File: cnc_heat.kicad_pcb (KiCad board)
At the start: 2 copper layers, 56.4 x 80 mm, 55 parts, among them J1 Raspberry_Pi_2_3, J2 DB25_Receptacle_MountingHoles, U1 74LVC1T45, U10 74LVC1T45, U11 74LVC1T45, U12 74LVC1T45, U13 74LVC1T45, U14 74LVC1T45, U15 74LVC1T45, U16 74LVC1T45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

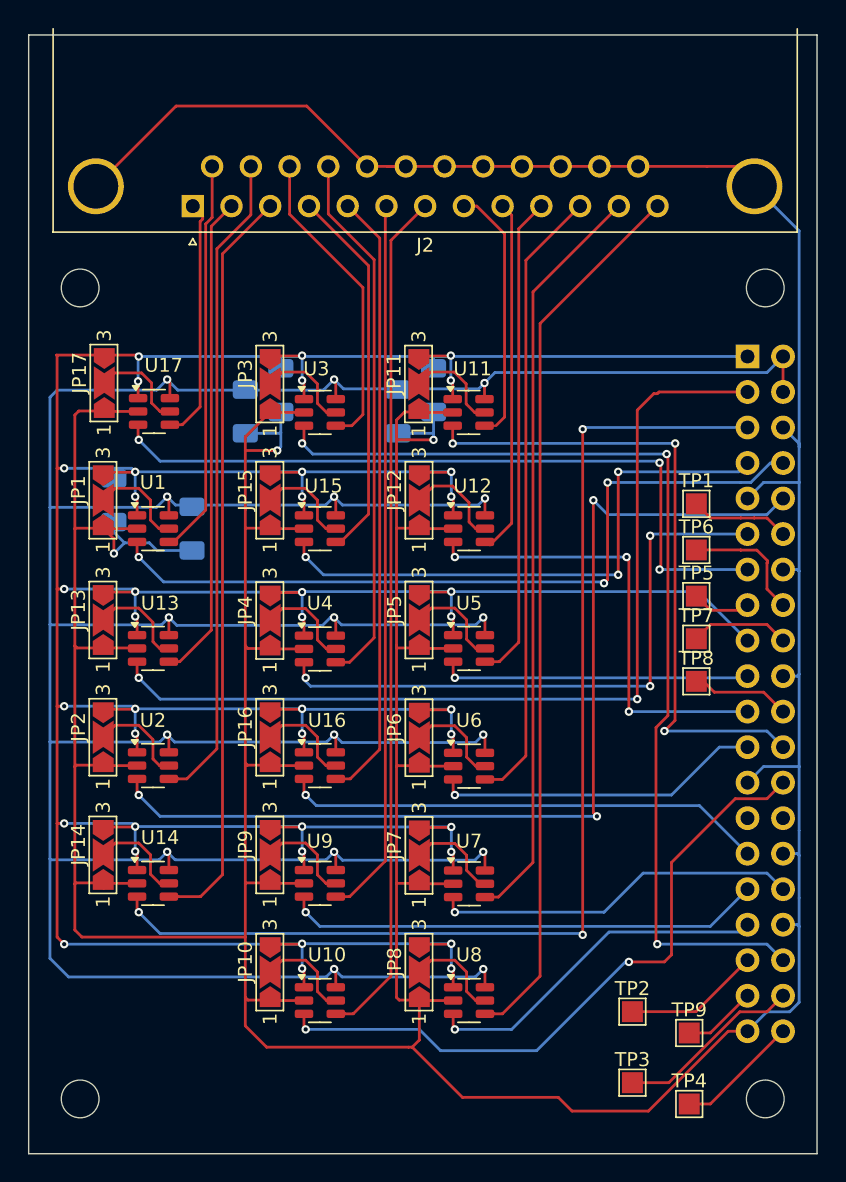
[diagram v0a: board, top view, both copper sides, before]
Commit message: routing cleanup
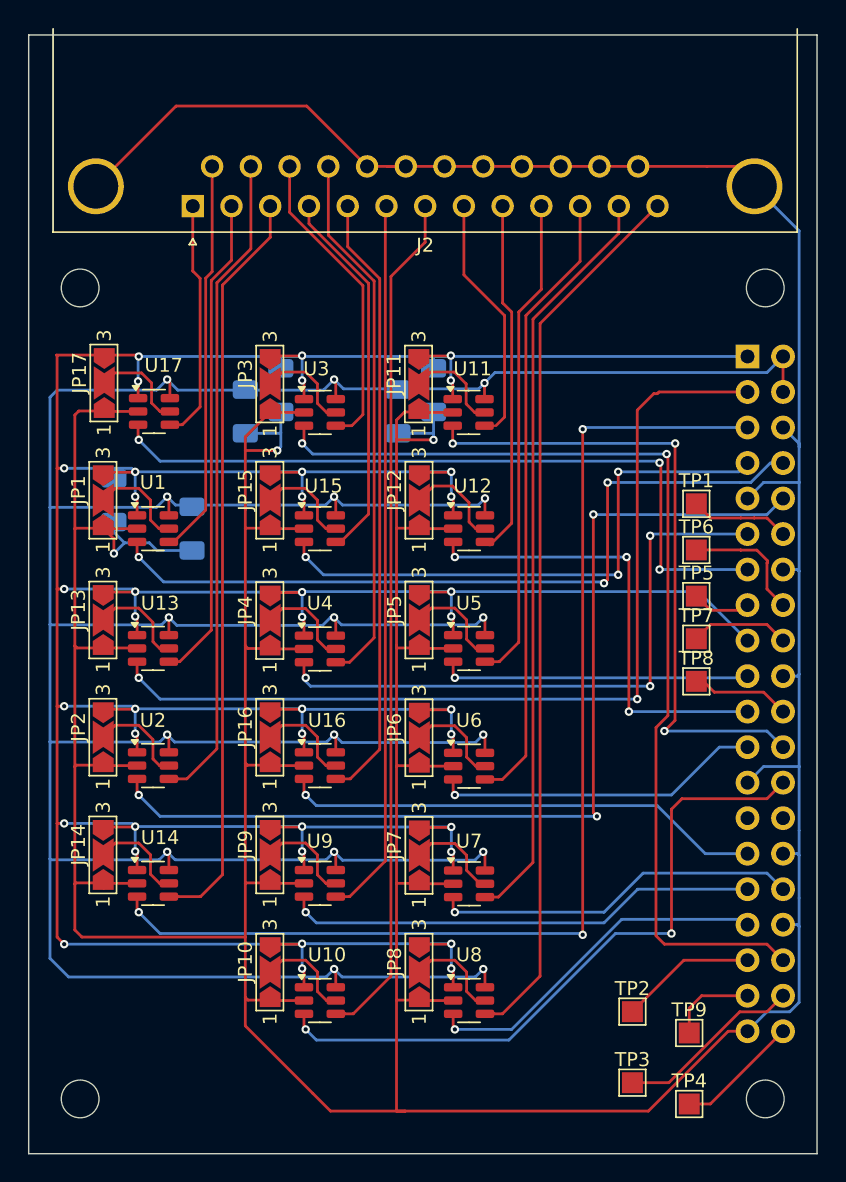
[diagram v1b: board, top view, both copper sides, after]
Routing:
- net GND: track 408.9 -> 414.0 mm
- net 15A: track 71.8 -> 70.3 mm
- net Net-(J1-GPIO26): track 5.27 -> 6.31 mm
- net 7A: track 47.7 -> 48.5 mm
- net 8B: track 18.4 -> 17.8 mm
- net 16A: track 72.7 -> 72.4 mm, vias 3 -> 2

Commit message: ocd routing
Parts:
- moved C6 43.1 mm to (77.5, 98.0)
- moved C5 37.5 mm to (77.5, 89.7)
- moved C4 24.4 mm to (77.5, 81.3)
- moved C3 18.1 mm to (77.5, 72.9)
- moved C1 10.6 mm to (77.5, 55.9)
- moved TP2 5.79 mm to (111.5, 96.3)
- moved TP3 5.11 mm to (111.5, 102.6)
- moved C2 2.27 mm to (77.5, 64.3)
- moved TP9 2.09 mm to (111.5, 99.3)
- moved TP4 0.92 mm to (111.5, 105.7)
- renumbered C5 to C1, C1 to C2, C6 to C3, C2 to C4, C7 to C5, C3 to C6
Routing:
- net GND: track 414.0 -> 405.3 mm, vias 3 -> 6
- net +5V: track 281.7 -> 288.1 mm
- net Net-(J1-GPIO19/MISO1): track 9.76 -> 3.71 mm
- net Net-(J1-GPIO20/MOSI1): track 13.3 -> 7.83 mm
- net 13B: track 64.3 -> 66.9 mm
- net Net-(J1-GPIO26): track 6.31 -> 3.92 mm
- net +3V3: track 348.8 -> 347.2 mm
- net 12B: track 53.9 -> 55.3 mm
- net 16A: track 72.4 -> 71.1 mm
- net 9B: track 25.5 -> 26.7 mm
- net 8A: track 47.0 -> 45.8 mm
- net 7B: track 61.8 -> 62.8 mm
- net 6B: track 51.5 -> 52.5 mm
- net Net-(JP2-C): track 7.06 -> 8.04 mm
- net Net-(JP14-C): track 7.06 -> 7.90 mm
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
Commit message: ocd routing
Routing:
- net 1A: track 53.7 -> 52.9 mm
- net 14A: track 55.9 -> 55.3 mm
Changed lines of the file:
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@@
 	)
 	(segment
-		(start 72.009 68.834)
-		(end 71.628 68.453)
+		(start 104.14 68.834)
+		(end 73.152 68.834)
 		(width 0.2)
 		(layer "B.Cu")
@@
 	)
 	(segment
-		(start 104.14 68.834)
-		(end 72.009 68.834)
+		(start 73.152 68.834)
+		(end 71.628 67.31)
 		(width 0.2)
 		(layer "B.Cu")
@@
 		(start 115.402346 61.974)
 		(end 116.792346 60.584)
-		(width 0.2)
-		(layer "B.Cu")
-		(net 6)
-	)
-	(segment
-		(start 71.628 68.453)
-		(end 71.628 67.31)
 		(width 0.2)
 		(layer "B.Cu")
@@
 	(segment
 		(start 107.95 60.452)
-		(end 71.882 60.452)
+		(end 73.152 60.452)
 		(width 0.2)
 		(layer "B.Cu")
@@
 	)
 	(segment
-		(start 71.882 60.452)
-		(end 71.628 60.198)
-		(width 0.2)
-		(layer "B.Cu")
-		(net 7)
-	)
-	(segment
-		(start 71.628 60.198)
+		(start 73.152 60.452)
 		(end 71.628 58.928)
 		(width 0.2)
